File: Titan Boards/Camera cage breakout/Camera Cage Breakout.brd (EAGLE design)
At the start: 100 x 80 mm, 5 parts

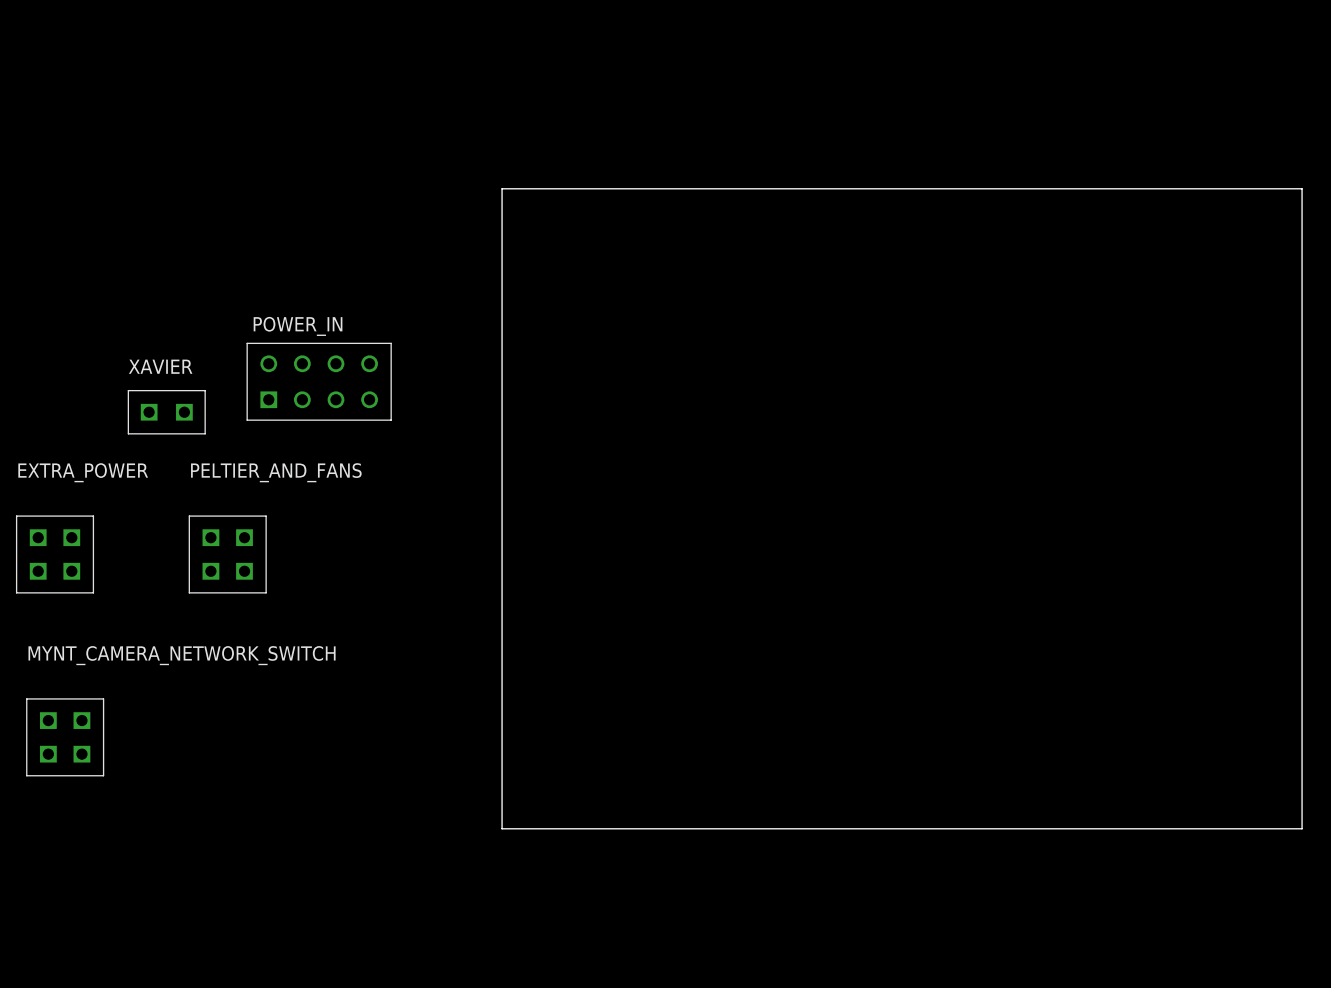
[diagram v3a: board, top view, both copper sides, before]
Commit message: schematic work for camera cage breakout
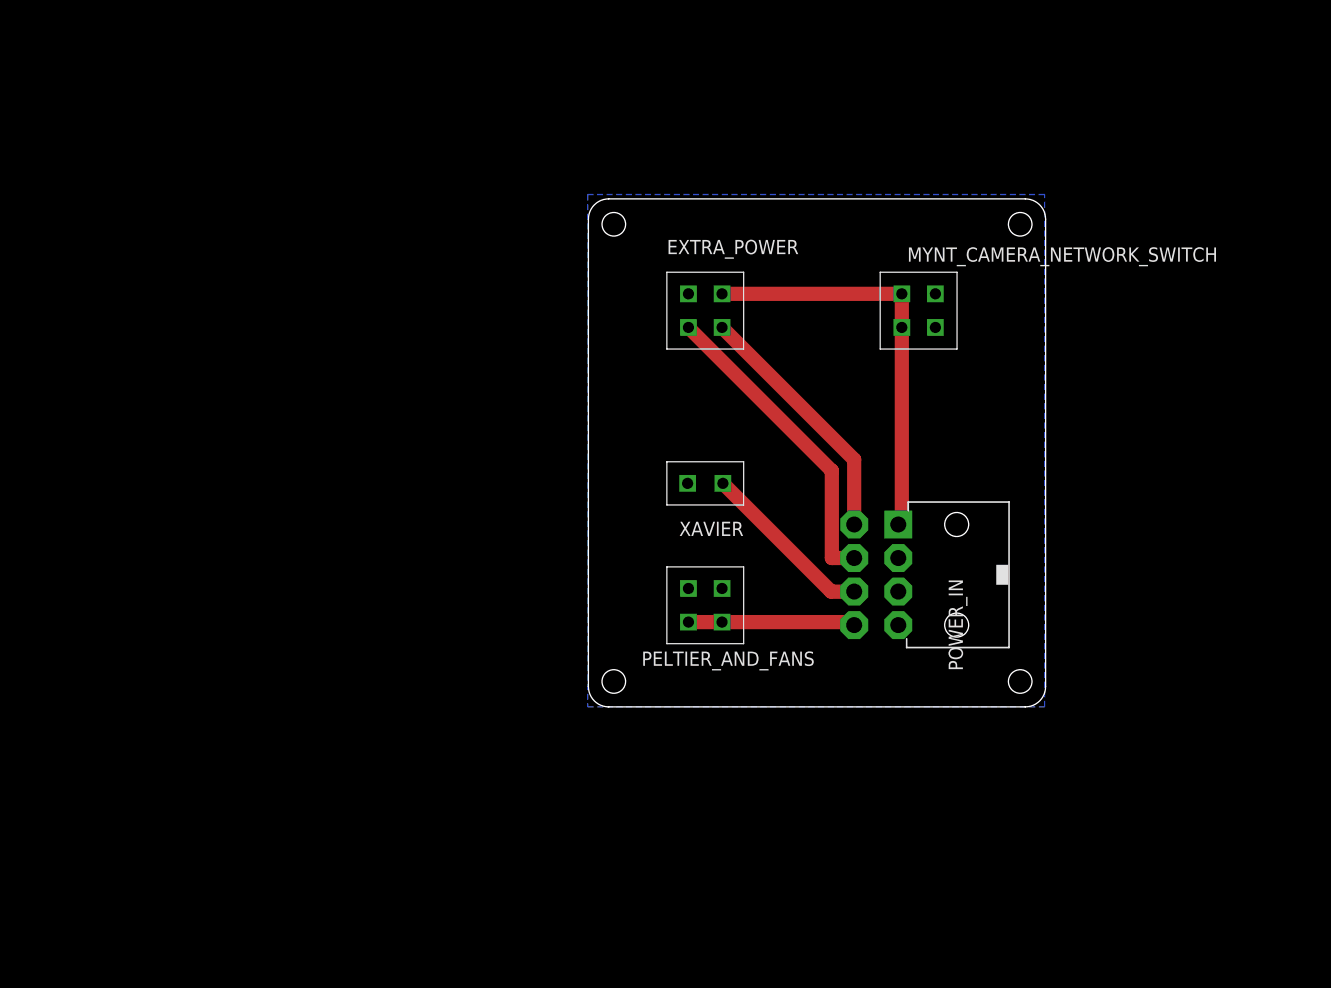
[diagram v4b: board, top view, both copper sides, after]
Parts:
- POWER_IN: value 8PIN_VERT -> 39-30-08?; device Vertical_Connectors:8PIN_VERT -> con-molex-mini-fit:39-30-?08?
- moved MYNT_CAMERA_NETWORK_SWITCH 119.3 mm to (52.1, 64.8), turned to 90 degrees
- moved EXTRA_POWER 86.8 mm to (25.4, 64.8)
- moved POWER_IN 76.3 mm to (49.5, 31.8), turned to 90 degrees
- moved XAVIER 67.9 mm to (25.4, 43.2), turned to 180 degrees
- moved PELTIER_AND_FANS 60.0 mm to (25.4, 27.9), turned to 180 degrees
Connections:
- removed net N$7: POWER_IN.P$4
- net 12V: now also EXTRA_POWER.P$3, POWER_IN.5; no longer EXTRA_POWER.P$1, POWER_IN.P$5
- net 3.3V: now also EXTRA_POWER.P$4, POWER_IN.6; no longer EXTRA_POWER.P$3, POWER_IN.P$7
- net 5V: now also POWER_IN.1; no longer POWER_IN.P$6
- net GND: now also EXTRA_POWER.P$1, POWER_IN.2, POWER_IN.3, POWER_IN.4; no longer EXTRA_POWER.P$4, POWER_IN.P$3, POWER_IN.P$8
- net PELTIER_SWITCHED: now also POWER_IN.8; no longer POWER_IN.P$2
- net XAVIER_SWITCHED: now also POWER_IN.7; no longer POWER_IN.P$1
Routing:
- net 5V: track 0.00 -> 51.5 mm
- net 3.3V: track 0.00 -> 39.0 mm
- net 12V: track 0.00 -> 31.5 mm
- net XAVIER_SWITCHED: track 0.00 -> 22.0 mm
- net PELTIER_SWITCHED: track 0.00 -> 20.9 mm
- added copper zone on layer 16, net GND
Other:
- board size 100 x 80 mm -> 57.1 x 63.5 mm
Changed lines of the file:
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@@
 <board>
 <plain>
-<wire x1="0" y1="0" x2="100" y2="0" width="0" layer="20"/>
-<wire x1="100" y1="0" x2="100" y2="80" width="0" layer="20"/>
-<wire x1="100" y1="80" x2="0" y2="80" width="0" layer="20"/>
-<wire x1="0" y1="80" x2="0" y2="0" width="0" layer="20"/>
+<circle x="64.77" y="18.415" radius="1.4732" width="0.025" layer="20"/>
+<circle x="13.97" y="18.415" radius="1.4732" width="0.025" layer="20"/>
+<circle x="13.97" y="75.565" radius="1.4732" width="0.025" layer="20"/>
+<circle x="64.77" y="75.565" radius="1.4732" width="0.025" layer="20"/>
+<wire x1="67.945" y1="76.2" x2="67.945" y2="17.78" width="0.025" layer="20"/>
+<wire x1="65.405" y1="15.24" x2="13.335" y2="15.24" width="0.025" layer="20"/>
+<wire x1="10.795" y1="76.2" x2="10.795" y2="17.78" width="0.025" layer="20"/>
+<wire x1="65.405" y1="78.74" x2="13.335" y2="78.74" width="0.025" layer="20"/>
+<wire x1="65.405" y1="15.24" x2="67.945" y2="17.78" width="0.025" layer="20" curve="90"/>
+<wire x1="10.795" y1="17.78" x2="13.335" y2="15.24" width="0.025" layer="20" curve="90"/>
+<wire x1="13.335" y1="78.74" x2="10.795" y2="76.2" width="0.025" layer="20" curve="90"/>
+<wire x1="67.945" y1="76.2" x2="65.405" y2="78.74" width="0.025" layer="20" curve="90"/>
 </plain>
 <attributes>
@@
 </autorouter>
 <elements>
-<element name="EXTRA_POWER" library="Vertical_Connectors" package="4PIN-VERT" value="4PIN-VERT" x="-55.88" y="34.29" smashed="yes">
-<attribute name="NAME" x="-60.68" y="43.89" size="1.778" layer="25"/>
-<attribute name="VALUE" x="-60.68" y="24.69" size="1.778" layer="27"/>
-</element>
-<element name="MYNT_CAMERA_NETWORK_SWITCH" library="Vertical_Connectors" package="4PIN-VERT" value="4PIN-VERT" x="-54.61" y="11.43" smashed="yes">
-<attribute name="NAME" x="-59.41" y="21.03" size="1.778" layer="25"/>
-<attribute name="VALUE" x="-59.41" y="1.83" size="1.778" layer="27"/>
-</element>
-<element name="PELTIER_AND_FANS" library="Vertical_Connectors" package="4PIN-VERT" value="4PIN-VERT" x="-34.29" y="34.29" smashed="yes">
-<attribute name="NAME" x="-39.09" y="43.89" size="1.778" layer="25"/>
-<attribute name="VALUE" x="-39.09" y="24.69" size="1.778" layer="27"/>
-</element>
-<element name="POWER_IN" library="Vertical_Connectors" package="8PIN_VERT" value="8PIN_VERT" x="-22.86" y="55.88" smashed="yes">
-<attribute name="NAME" x="-31.26" y="62.18" size="1.778" layer="25"/>
-<attribute name="VALUE" x="-31.26" y="47.48" size="1.778" layer="27"/>
-</element>
-<element name="XAVIER" library="Vertical_Connectors" package="2PIN-VERT" value="2PIN-VERT" x="-41.91" y="52.07" smashed="yes">
-<attribute name="NAME" x="-46.71" y="56.87" size="1.778" layer="25"/>
-<attribute name="VALUE" x="-46.71" y="47.27" size="1.778" layer="27"/>
+<element name="EXTRA_POWER" library="Vertical_Connectors" package="4PIN-VERT" value="4PIN-VERT" x="25.4" y="64.77" smashed="yes">
+<attribute name="NAME" x="20.6" y="71.83" size="1.778" layer="25"/>
+<attribute name="VALUE" x="20.6" y="57.71" size="1.778" layer="27"/>
+</element>
+<element name="MYNT_CAMERA_NETWORK_SWITCH" library="Vertical_Connectors" package="4PIN-VERT" value="4PIN-VERT" x="52.07" y="64.77" smashed="yes" rot="R90">
+<attribute name="NAME" x="89.46" y="72.67" size="1.778" layer="25" rot="R180"/>
+<attribute name="VALUE" x="56.87" y="59.13" size="1.778" layer="27" rot="R180"/>
+</element>
+<element name="PELTIER_AND_FANS" library="Vertical_Connectors" package="4PIN-VERT" value="4PIN-VERT" x="25.4" y="27.94" smashed="yes" rot="R180">
+<attribute name="NAME" x="39.09" y="22.15" size="1.778" layer="25" rot="R180"/>
+<attribute name="VALUE" x="31.47" y="35" size="1.778" layer="27" rot="R180"/>
+</element>
+<element name="POWER_IN" library="con-molex-mini-fit" package="39-30-?08?" value="39-30-08?" x="49.53" y="31.75" smashed="yes" rot="R90">
+<attribute name="NAME" x="55.83" y="31.26" size="1.778" layer="25" rot="R270"/>
+</element>
+<element name="XAVIER" library="Vertical_Connectors" package="2PIN-VERT" value="2PIN-VERT" x="25.4" y="43.18" smashed="yes" rot="R180">
+<attribute name="NAME" x="30.2" y="38.38" size="1.778" layer="25" rot="R180"/>
+<attribute name="VALUE" x="30.2" y="47.98" size="1.778" layer="27" rot="R180"/>
 </element>
 </elements>
 <signals>
-<signal name="GND">
+<signal name="GND" airwireshidden="yes">
 <contactref element="MYNT_CAMERA_NETWORK_SWITCH" pad="P$3"/>
 <contactref element="MYNT_CAMERA_NETWORK_SWITCH" pad="P$4"/>
@@
 <contactref element="PELTIER_AND_FANS" pad="P$4"/>
 <contactref element="XAVIER" pad="P$2"/>
-<contactref element="POWER_IN" pad="P$8"/>
-<contactref element="EXTRA_POWER" pad="P$4"/>
-<contactref element="POWER_IN" pad="P$3"/>
-<wire x1="-52.51" y1="9.33" x2="-56.71" y2="9.33" width="0" layer="19" extent="1-1"/>
-<wire x1="-57.98" y1="32.19" x2="-56.71" y2="9.33" width="0" layer="19" extent="1-1"/>
-<wire x1="-36.39" y1="32.19" x2="-57.98" y2="32.19" width="0" layer="19" extent="1-1"/>
-<wire x1="-32.19" y1="32.19" x2="-36.39" y2="32.19" width="0" layer="19" extent="1-1"/>
-<wire x1="-39.70331875" y1="52.07" x2="-36.39" y2="32.19" width="0" layer="19" extent="1-1"/>
-<wire x1="-24.96" y1="58.13" x2="-39.70331875" y2="52.07" width="0" layer="19" extent="1-1"/>
-<wire x1="-20.76" y1="53.63" x2="-24.96" y2="58.13" width="0" layer="19" extent="1-1"/>
+<polygon width="0.254" layer="16" thermals="no" rank="2">
+<vertex x="10.704284375" y="79.284284375"/>
+<vertex x="10.704284375" y="15.24"/>
+<vertex x="67.824046875" y="15.24"/>
+<vertex x="67.824046875" y="79.284284375"/>
+</polygon>
+<contactref element="POWER_IN" pad="4"/>
+<contactref element="POWER_IN" pad="2"/>
+<contactref element="EXTRA_POWER" pad="P$1"/>
+<contactref element="POWER_IN" pad="3"/>
 </signal>
 <signal name="5V">
 <contactref element="MYNT_CAMERA_NETWORK_SWITCH" pad="P$1"/>
 <contactref element="MYNT_CAMERA_NETWORK_SWITCH" pad="P$2"/>
-<contactref element="POWER_IN" pad="P$6"/>
 <contactref element="EXTRA_POWER" pad="P$2"/>
-<wire x1="-52.51" y1="13.53" x2="-56.71" y2="13.53" width="0" layer="19" extent="1-1"/>
-<wire x1="-53.78" y1="36.39" x2="-52.51" y2="13.53" width="0" layer="19" extent="1-1"/>
-<wire x1="-16.56" y1="53.63" x2="-53.78" y2="36.39" width="0" layer="19" extent="1-1"/>
+<wire x1="49.97" y1="62.67" x2="49.97" y2="66.87" width="1.778" layer="1"/>
+<wire x1="49.97" y1="66.87" x2="27.5" y2="66.87" width="1.778" layer="1"/>
+<contactref element="POWER_IN" pad="1"/>
+<wire x1="49.97" y1="62.67" x2="49.97" y2="38.4765" width="1.778" layer="1"/>
+<wire x1="49.97" y1="38.4765" x2="49.53" y2="38.0365" width="1.778" layer="1"/>
 </signal>
 <signal name="PELTIER_SWITCHED">
 <contactref element="PELTIER_AND_FANS" pad="P$1"/>
 <contactref element="PELTIER_AND_FANS" pad="P$2"/>
-<contactref element="POWER_IN" pad="P$2"/>
-<wire x1="-32.19" y1="36.39" x2="-29.16" y2="58.13" width="0" layer="19" extent="1-1"/>
-<wire x1="-36.39" y1="36.39" x2="-32.19" y2="36.39" width="0" layer="19" extent="1-1"/>
+<wire x1="27.5" y1="25.84" x2="23.3" y2="25.84" width="1.778" layer="1"/>
+<contactref element="POWER_IN" pad="8"/>
+<wire x1="44.0182" y1="25.4635" x2="43.6417" y2="25.84" width="1.778" layer="1"/>
+<wire x1="43.6417" y1="25.84" x2="27.5" y2="25.84" width="1.778" layer="1"/>
 </signal>
 <signal name="XAVIER_SWITCHED">
 <contactref element="XAVIER" pad="P$1"/>
-<contactref element="POWER_IN" pad="P$1"/>
-<wire x1="-44.11668125" y1="52.07" x2="-29.16" y2="53.63" width="0" layer="19" extent="1-1"/>
+<contactref element="POWER_IN" pad="7"/>
+<wire x1="44.0182" y1="29.6545" x2="41.13218125" y2="29.6545" width="1.778" layer="1"/>
+<wire x1="41.13218125" y1="29.6545" x2="27.60668125" y2="43.18" width="1.778" layer="1"/>
 </signal>
 <signal name="12V">
-<contactref element="POWER_IN" pad="P$5"/>
-<contactref element="EXTRA_POWER" pad="P$1"/>
-<wire x1="-57.98" y1="36.39" x2="-16.56" y2="58.13" width="0" layer="19" extent="1-1"/>
+<contactref element="EXTRA_POWER" pad="P$3"/>
+<contactref element="POWER_IN" pad="5"/>
+<wire x1="27.5" y1="62.67" x2="44.0182" y2="46.1518" width="1.778" layer="1"/>
+<wire x1="44.0182" y1="46.1518" x2="44.0182" y2="38.0365" width="1.778" layer="1"/>
 </signal>
 <signal name="3.3V">
-<contactref element="POWER_IN" pad="P$7"/>
-<contactref element="EXTRA_POWER" pad="P$3"/>
-<wire x1="-53.78" y1="32.19" x2="-24.96" y2="53.63" width="0" layer="19" extent="1-1"/>
-</signal>
-<signal name="N$7">
-<contactref element="POWER_IN" pad="P$4"/>
+<contactref element="EXTRA_POWER" pad="P$4"/>
+<contactref element="POWER_IN" pad="6"/>
+<wire x1="41.2268" y1="33.8455" x2="44.0182" y2="33.8455" width="1.778" layer="1"/>
+<wire x1="23.3" y1="62.67" x2="41.2268" y2="44.7432" width="1.778" layer="1"/>
+<wire x1="41.2268" y1="44.7432" x2="41.2268" y2="33.8455" width="1.778" layer="1"/>
 </signal>
 </signals>

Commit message: final camera cage breakout with gerbers
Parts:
- removed MYNT_CAMERA_NETWORK_SWITCH, PELTIER_AND_FANS: 4PIN-VERT, Vertical_Connectors:4PIN-VERT
- added MYNT_CAMERA, PLTA_FANS: 4PIN-VERT, Vertical_Connectors:4PIN-VERT
- added U$1: CAMERA_CAGE_TEST, 3M_929852_Connector:6-PIN
- moved POWER_IN 5.24 mm to (48.3, 36.8)
- moved EXTRA_POWER 1.65 mm to (23.7, 64.8)
- moved XAVIER 1.65 mm to (23.7, 43.2)
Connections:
- net 12V: now also U$1.P$3
- net 3.3V: now also U$1.P$4
- net 5V: now also MYNT_CAMERA.P$1, MYNT_CAMERA.P$2, U$1.P$2; no longer MYNT_CAMERA_NETWORK_SWITCH.P$1, MYNT_CAMERA_NETWORK_SWITCH.P$2
- net GND: now also MYNT_CAMERA.P$3, MYNT_CAMERA.P$4, PLTA_FANS.P$3, PLTA_FANS.P$4, U$1.P$1; no longer MYNT_CAMERA_NETWORK_SWITCH.P$3, MYNT_CAMERA_NETWORK_SWITCH.P$4, PELTIER_AND_FANS.P$3, PELTIER_AND_FANS.P$4
- net PELTIER_SWITCHED: now also PLTA_FANS.P$1, PLTA_FANS.P$2, U$1.P$6; no longer PELTIER_AND_FANS.P$1, PELTIER_AND_FANS.P$2
- net XAVIER_SWITCHED: now also U$1.P$5
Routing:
- net 12V: track 31.5 -> 52.1 mm
- net 5V: track 51.5 -> 70.5 mm
- net 3.3V: track 39.0 -> 51.7 mm
- net XAVIER_SWITCHED: track 22.0 -> 32.1 mm
- net PELTIER_SWITCHED: track 20.9 -> 29.8 mm
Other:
- board text added: "12V"
- board text added: "3.3.V"
- board text added: "3.3V"
- board text added: "5V"
- board text added: "GND"
- board text added: "NETWORK_SW"
- board text added: "PLTA_SW"
- board text added: "XV_SW"
